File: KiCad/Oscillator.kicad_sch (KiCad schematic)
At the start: 38 parts, among them Q1 NPN, Q2 PNP, Q3 PNP, Q4 NPN, U1 40106, U3 TL074, U4 40106, U6 TL074

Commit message: unified kicad projects, added footprints
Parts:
- removed J_In, J_Out: Screw_Terminal_01x01, symbol Connector:Screw_Terminal_01x01
- C4: renamed from C1; footprint (none) -> Capacitor_THT:C_Rect_L18.0mm_W7.0mm_P15.00mm_FKS3_FKP3
- C5: renamed from C2; footprint (none) -> Capacitor_THT:C_Rect_L18.0mm_W7.0mm_P15.00mm_FKS3_FKP3
- C6: renamed from C3; footprint (none) -> Capacitor_THT:C_Rect_L7.5mm_W6.5mm_P5.00mm
- Q5: renamed from Q2; footprint (none) -> Package_TO_SOT_THT:TO-92
- Q6: renamed from Q3; footprint (none) -> Package_TO_SOT_THT:TO-92
- Q7: renamed from Q1; footprint (none) -> Package_TO_SOT_THT:TO-92
- Q8: renamed from Q4; footprint (none) -> Package_TO_SOT_THT:TO-92
- R13: renamed from R_Coarse1; footprint (none) -> Resistor_SMD:R_0201_0603Metric
- R14: renamed from R_Fine1; footprint (none) -> Resistor_SMD:R_0201_0603Metric
- R15: renamed from R_In1; footprint (none) -> Resistor_SMD:R_0201_0603Metric
- R16: renamed from R_Coarse2; footprint (none) -> Resistor_SMD:R_0201_0603Metric
- R17: renamed from R_Fine2; footprint (none) -> Resistor_SMD:R_0201_0603Metric
- R18: renamed from R_In2; footprint (none) -> Resistor_SMD:R_0201_0603Metric
- R19: renamed from R1; footprint (none) -> Resistor_SMD:R_0201_0603Metric
- R20: renamed from R2; footprint (none) -> Resistor_SMD:R_0201_0603Metric
- R21: renamed from R5; footprint (none) -> Resistor_SMD:R_0201_0603Metric
- R22: renamed from R4; footprint (none) -> Resistor_SMD:R_0201_0603Metric
- R23: renamed from R3; footprint (none) -> Resistor_SMD:R_0201_0603Metric
- R24: renamed from R6; footprint (none) -> Resistor_SMD:R_0201_0603Metric
- RV10: renamed from RV_Mixer; footprint (none) -> Potentiometer 51CAD_E24_A20L:POT_51CAD_12P5X13P25_BRN
- RV6: renamed from RV_CoarseTuning1; footprint (none) -> Potentiometer 51CAD_E24_A20L:POT_51CAD_12P5X13P25_BRN
- RV7: renamed from RV_FineTuning1; footprint (none) -> Potentiometer 51CAD_E24_A20L:POT_51CAD_12P5X13P25_BRN
- RV8: renamed from RV_CoarseTuning2; footprint (none) -> Potentiometer 51CAD_E24_A20L:POT_51CAD_12P5X13P25_BRN
- RV9: renamed from RV_FineTuning2; footprint (none) -> Potentiometer 51CAD_E24_A20L:POT_51CAD_12P5X13P25_BRN
- TH10: renamed from TH_Coarse2; footprint (none) -> Resistor_SMD:R_0201_0603Metric
- TH11: renamed from TH_Fine2; footprint (none) -> Resistor_SMD:R_0201_0603Metric
- TH12: renamed from TH_In2; footprint (none) -> Resistor_SMD:R_0201_0603Metric
- TH7: renamed from TH_Coarse1; footprint (none) -> Resistor_SMD:R_0201_0603Metric
- TH8: renamed from TH_Fine1; footprint (none) -> Resistor_SMD:R_0201_0603Metric
- TH9: renamed from TH_In1; footprint (none) -> Resistor_SMD:R_0201_0603Metric
- U3: renamed from U4; footprint (none) -> Schmitt Inv. CD40106BE:N14
- U3: renamed from U1; footprint (none) -> Schmitt Inv. CD40106BE:N14
- U4: renamed from U6; footprint (none) -> Op Amp TL074CD:SOIC_074CD_STM
- U4: renamed from U3; footprint (none) -> Op Amp TL074CD:SOIC_074CD_STM
- renumbered D1 to D3, D2 to D4
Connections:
- net Mix In 2: now also U3.3; no longer U3.1
- net at D4.2 (A): now also U3.4; no longer U3.2
- net at R22.2, R23.1: now also U4.6 (-); no longer U4.2 (-)
- net at R23.2, R24.1: now also U4.7; no longer U4.1
- net at C6.2, R21.1: now also U4.5 (+); no longer U4.3 (+)
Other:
- note added: "Coarse Tuning 1"
- note added: "Coarse Tuning 2"
- note added: "Fine Tuning 1"
- note added: "Fine Tuning 2"

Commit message: renamed main schematic file, annotations start at 0
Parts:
- renumbered C4 to C1, C5 to C2, C6 to C3, D3 to D1, D4 to D2, Q5 to Q1, Q6 to Q2, Q7 to Q3, Q8 to Q4, R13 to R1, R22 to R10, R23 to R11, R24 to R12, R14 to R2, R15 to R3, R16 to R4, R17 to R5, R18 to R6, R19 to R7, R20 to R8, R21 to R9, RV6 to RV1, RV7 to RV2, RV8 to RV3, RV9 to RV4, RV10 to RV5, TH7 to TH1, TH8 to TH2, TH9 to TH3, TH10 to TH4, TH11 to TH5, TH12 to TH6, U3 to U1, U4 to U2

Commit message: amplifier sch., general changes to oscillator sch.
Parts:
- removed R12: 10k, Resistor_SMD:R_0201_0603Metric, symbol Device:R_US
- added R13: 1k, Resistor_SMD:R_0201_0603Metric, symbol Device:R_US
- added R9: 100k, symbol Device:R_US
- added unit 3 of U2
- added unit 4 of U2
- R10: value 33k -> 1k; footprint Resistor_SMD:R_0201_0603Metric -> (none)
- R12: renamed from R11; value 100k -> 1k
- renumbered R9 to R11
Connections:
- net GND: now also U2.3 (+), U2.5 (+); no longer R10.1
- net Mix In 1: now also U2.8, U2.9 (-); no longer C1.1, D1.1 (K), Q3.1 (C), U1.1
- net Mix In 2: now also U2.13 (-), U2.14; no longer C2.1, D2.1 (K), Q4.1 (C), U1.3
- net Out: now also U2.7, R13.1
- net at C3.1, U2.1: now also R10.2; no longer U2.2 (-)
- net at RV5.2: now also R9.1; no longer U2.3 (+)
- net at R12.2: now also U2.6 (-), R13.2; no longer U2.7
- net at C3.2, R11.1: now also R12.1; no longer U2.5 (+)
- net +12V renamed +9V
- net -12V renamed -9V
- new net: C1.1, D1.1 (K), Q3.1 (C), U1.1, U2.10 (+)
- new net: R10.1, R9.2, U2.2 (-)
- new net: C2.1, D2.1 (K), Q4.1 (C), U1.3, U2.12 (+)
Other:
- note added: "10mV pp., centered at 0V"
- moved on the sheet: C1, C2, C3, D1, D2, Q1, Q2, Q3, Q4, R11, R12, R4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

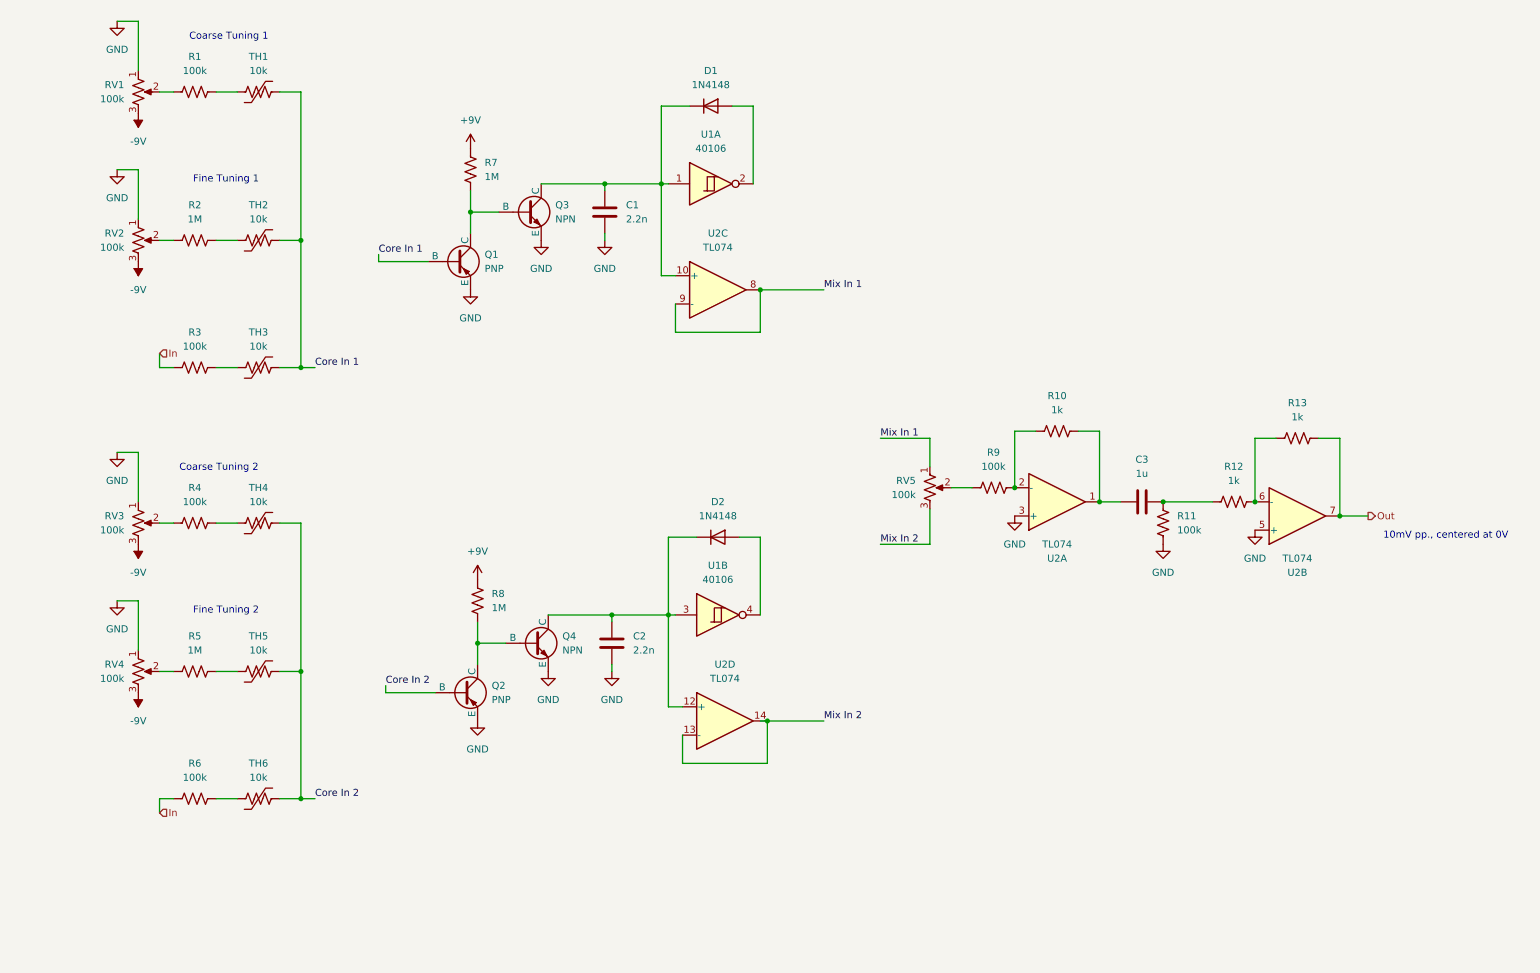
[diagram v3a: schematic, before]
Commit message: improved osc.'s output buffer cct., swap filter & amp
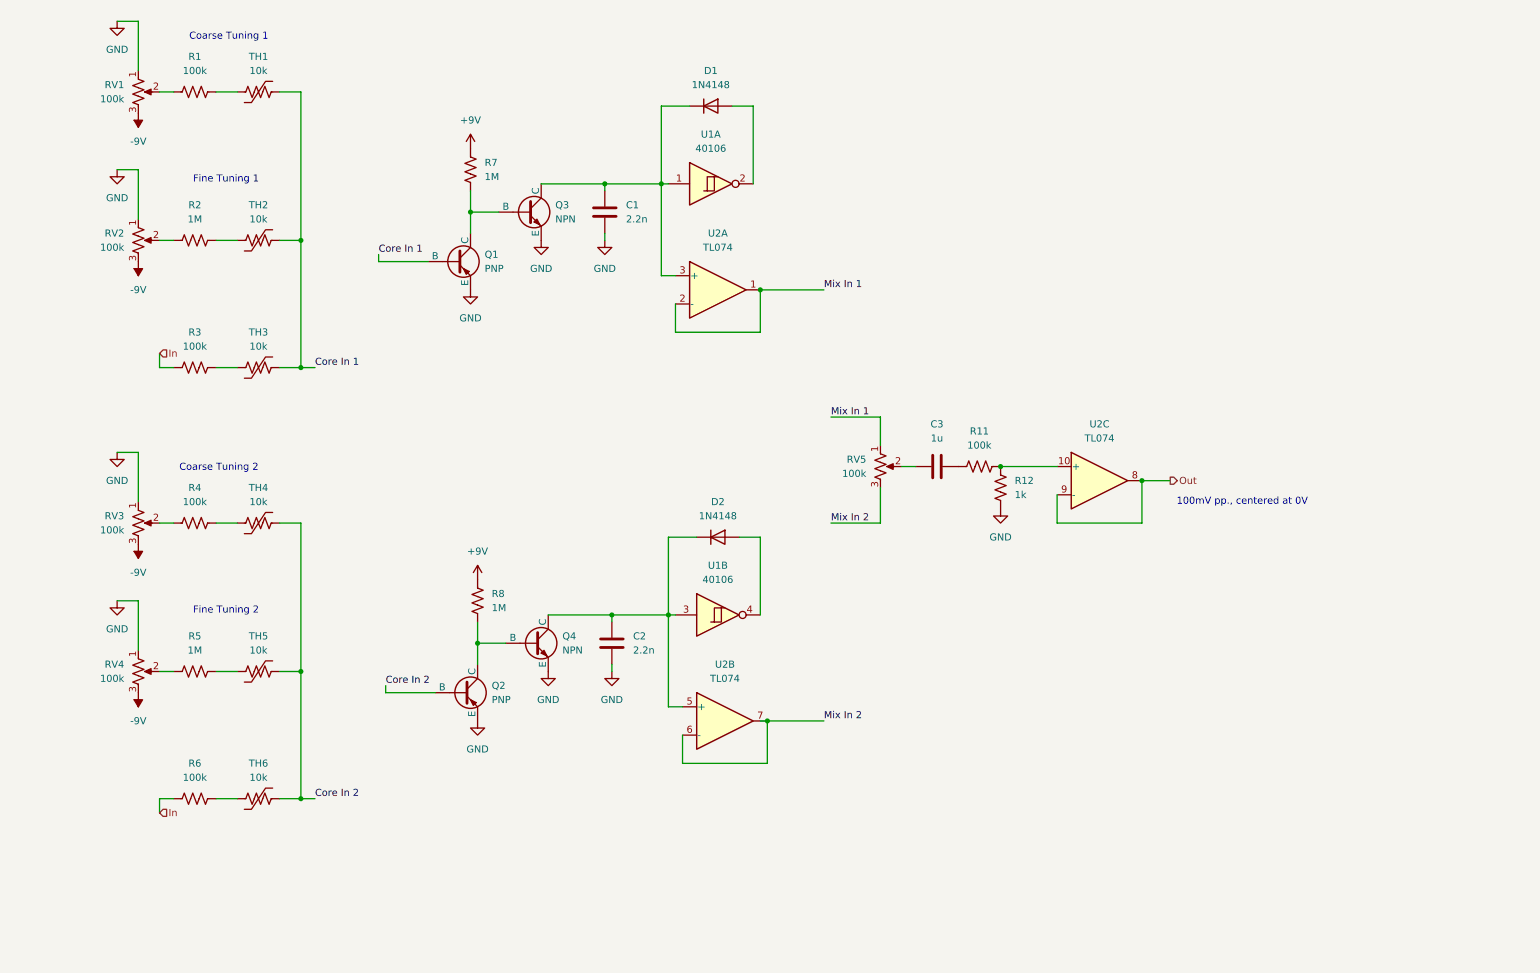
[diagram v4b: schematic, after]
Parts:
- removed R10: 1k, symbol Device:R_US
- removed R13: 1k, Resistor_SMD:R_0201_0603Metric, symbol Device:R_US
- removed R9: 100k, symbol Device:R_US
- removed unit 1 of U2
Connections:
- net GND: now also R12.1; no longer R11.2, U2.5 (+)
- net Mix In 1: now also U2.1, U2.2 (-); no longer U2.8, U2.9 (-)
- net Mix In 2: now also U2.6 (-), U2.7; no longer U2.13 (-), U2.14
- net Out: now also U2.8, U2.9 (-); no longer U2.7
- net at C1.1, D1.1 (K), Q3.1 (C)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: now also U2.3 (+); no longer U2.10 (+)
- net at C3.1: now also RV5.2
- net at C2.1, D2.1 (K), Q4.1 (C)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: now also U2.5 (+); no longer U2.12 (+)
- net at C3.2, R11.1: no longer R12.1
- net at R12.2: now also R11.2, U2.10 (+); no longer U2.6 (-)
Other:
- note added: "100mV pp., centered at 0V"
- note removed: "10mV pp., centered at 0V"
- moved on the sheet: C3, RV5, U2C

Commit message: added critical trimmer resistor that the osc. was missing
The trimmer resistor serves in a voltage divider to the osc.'s input signal. Without that voltage divider, the coarse tuning knob's range is too large (i.e. it's too coarse) and therefore unusable (according to the LTspice simualtions).
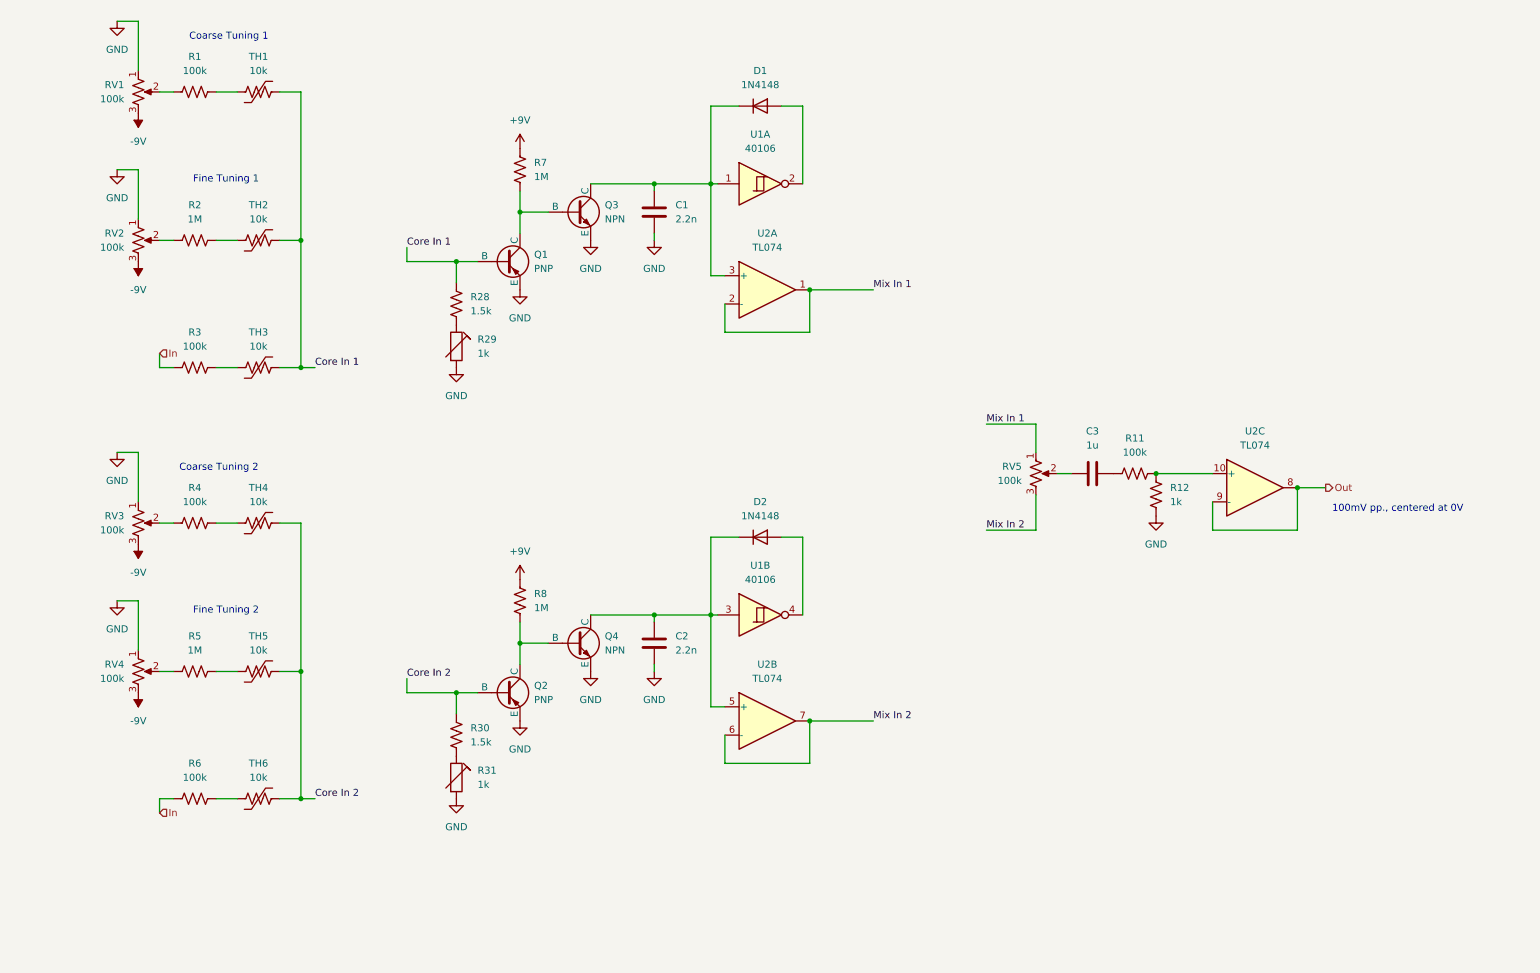
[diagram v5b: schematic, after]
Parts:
- added R28, R30: 1.5k, symbol Device:R_US
- added R29, R31: 1k, symbol Device:R_Trim
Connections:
- net Core In 1: now also R28.1
- net Core In 2: now also R30.1
- net GND: now also R29.2, R31.2
- new net: R30.2, R31.1
- new net: R28.2, R29.1
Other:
- moved on the sheet: C1, C2, C3, D1, D2, Q1, Q2, Q3, Q4, R11, R12, R7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

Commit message: drafted filter schematic
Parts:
- renumbered C3 to C2, C2 to C3, Q3 to Q1, Q1 to Q2, Q4 to Q3, Q2 to Q4, R8 to R10, R5 to R11, R30 to R12, R31 to R13, R6 to R14, R7 to R2, R2 to R3, R28 to R4, R29 to R5, R3 to R6, R11 to R7, R12 to R8, R4 to R9, RV5 to RV3, RV3 to RV4, RV4 to RV5
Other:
- moved on the sheet: C1, C3, D1, D2, Q1, Q2, Q3, Q4, R10, R12, R13, R2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

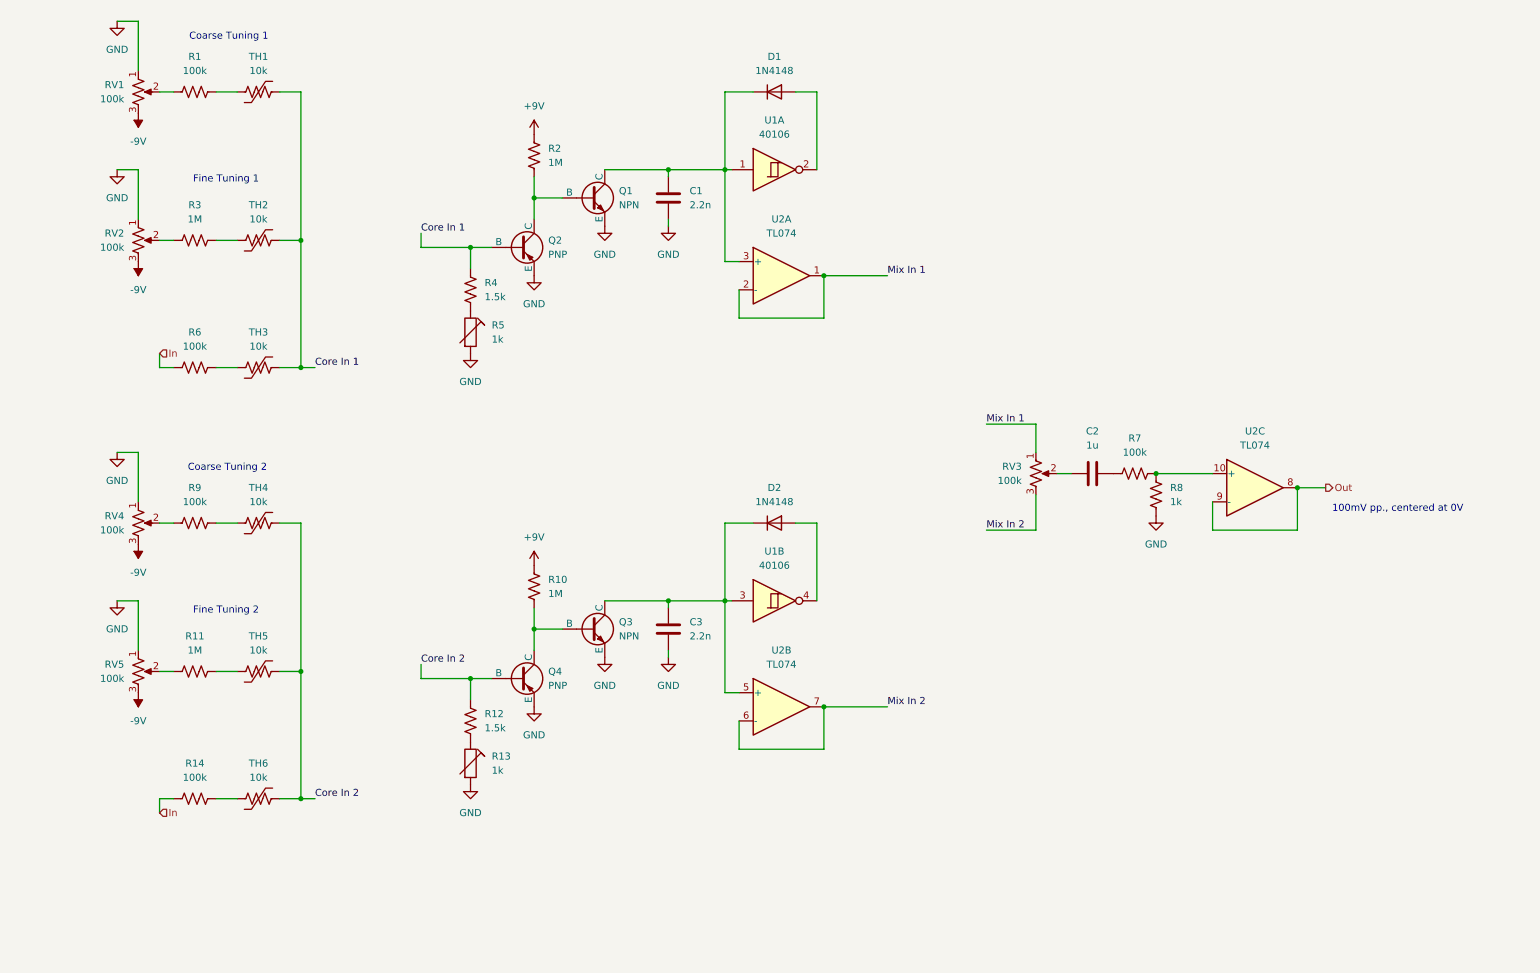
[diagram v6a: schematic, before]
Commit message: replaced some pots with voltage dividers, ltspice qol
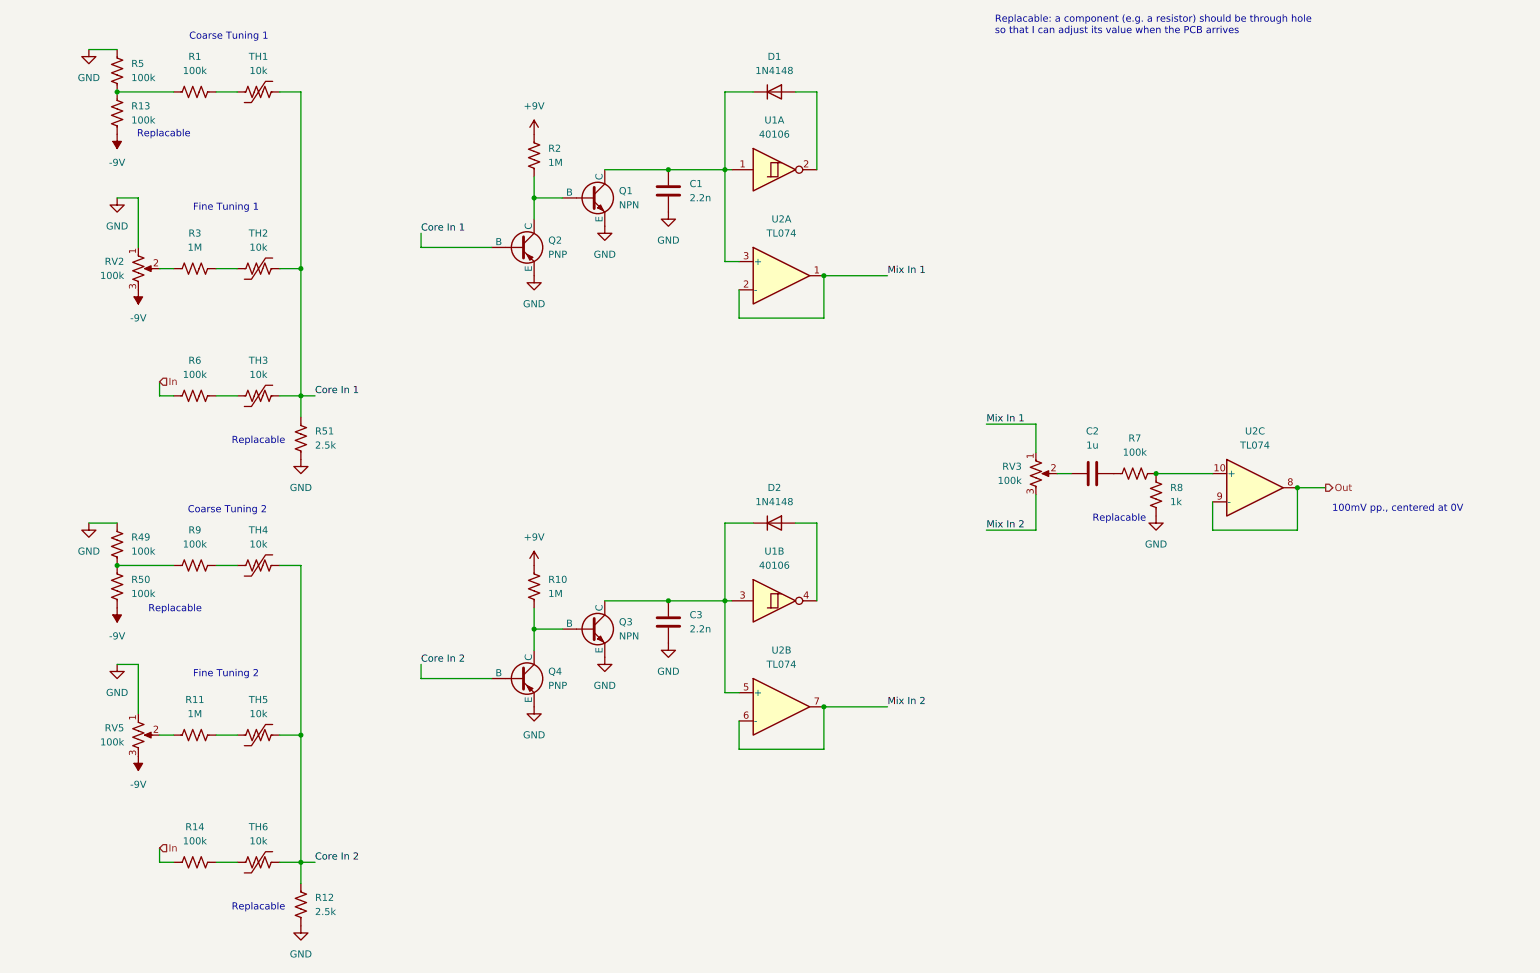
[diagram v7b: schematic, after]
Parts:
- removed R13, R5: 1k, symbol Device:R_Trim
- removed R4: 1.5k, symbol Device:R_US
- removed RV1, RV4: 100k, Potentiometer 51CAD_E24_A20L:POT_51CAD_12P5X13P25_BRN, symbol Device:R_Potentiometer_US
- added R13, R49, R5, R50: 100k, Resistor_SMD:R_0201_0603Metric, symbol Device:R_US
- added R51: 2.5k, symbol Device:R_US
- R12: value 1.5k -> 2.5k
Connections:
- net -9V: now also R13.1, R50.1
- net Core In 1: now also R51.1
- net GND: now also R12.2, R49.2, R5.2, R51.2
- net at R1.1: now also R13.2, R5.1
- net at R9.1: now also R49.1, R50.2
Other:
- note added: "Replacable"
- note added: "Replacable: a component (e.g. a resistor) should be through hole so that I can adjust its value when the PCB arrives"
- moved on the sheet: C1, C3, R11, R14, R3, R6, R9, RV2, RV5, TH2, TH3, TH4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
